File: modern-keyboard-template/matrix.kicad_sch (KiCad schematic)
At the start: 0 parts

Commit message: updated matrix and added dependencies
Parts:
- added D1, D10, D11, D12, D13, D14, D15, D16, D17, D18, D19, D2, D20, D21, D22, D23, D24, D25, D26, D27, D28, D29, D3, D30, D31, D32, D33, D34, D35, D36, D37, D38, D39, D4, D40, D41, D42, D43, D44, D45, D46, D47, D48, D49, D5, D50, D51, D52, D53, D54, D55, D56, D57, D58, D59, D6, D60, D61, D62, D63, D64, D65, D66, D67, D68, D69, D7, D70, D71, D72, D73, D74, D75, D76, D77, D78, D79, D8, D80, D81, D82, D83, D84, D9: D, Diode_SMD:D_SOD-123, symbol Device:D
- added SW? (x84): ~, switches:Kailh_socket_MX, symbol Switch:SW_Push
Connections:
- new net: D12.2 (A), SW?.1
- new net: D19.2 (A), SW?.1
- new net: D42.2 (A), SW?.1
- new net: D4.2 (A), SW?.1
- new net: D58.2 (A), SW?.1
- new net: D57.2 (A), SW?.1
- new net: D10.2 (A), SW?.1
- new net: D33.2 (A), SW?.1
- new net: D48.2 (A), SW?.1
- new net: D5.2 (A), SW?.1
- new net: D80.2 (A), SW?.1
- new net: D53.2 (A), SW?.1
- new net: D73.2 (A), SW?.1
- new net: D31.2 (A), SW?.1
- new net: D83.2 (A), SW?.1
- new net: D66.2 (A), SW?.1
- new net: D69.2 (A), SW?.1
- new net: D35.2 (A), SW?.1
- new net: D50.2 (A), SW?.1
- new net: D18.2 (A), SW?.1
- new net: D75.2 (A), SW?.1
- new net: D54.2 (A), SW?.1
- new net: D52.2 (A), SW?.1
- new net: D13.2 (A), SW?.1
- new net: D15.2 (A), SW?.1
- new net: D29.2 (A), SW?.1
- new net: D71.2 (A), SW?.1
- new net: D67.2 (A), SW?.1
- new net: D44.2 (A), SW?.1
- new net: D55.2 (A), SW?.1
- new net: D17.2 (A), SW?.1
- new net: D62.2 (A), SW?.1
- new net: D37.2 (A), SW?.1
- new net: D6.2 (A), SW?.1
- new net: D84.2 (A), SW?.1
- new net: D2.2 (A), SW?.1
- new net: D25.2 (A), SW?.1
- new net: D68.2 (A), SW?.1
- new net: D30.2 (A), SW?.1
- new net: D26.2 (A), SW?.1
- new net: D81.2 (A), SW?.1
- new net: D60.2 (A), SW?.1
- new net: D74.2 (A), SW?.1
- new net: D46.2 (A), SW?.1
- new net: D72.2 (A), SW?.1
- new net: D56.2 (A), SW?.1
- new net: D49.2 (A), SW?.1
- new net: D7.2 (A), SW?.1
- new net: D41.2 (A), SW?.1
- new net: D70.2 (A), SW?.1
- new net: D23.2 (A), SW?.1
- new net: D9.2 (A), SW?.1
- new net: D20.2 (A), SW?.1
- new net: D76.2 (A), SW?.1
- new net: D78.2 (A), SW?.1
- new net: D38.2 (A), SW?.1
- new net: D63.2 (A), SW?.1
- new net: D51.2 (A), SW?.1
- new net: D47.2 (A), SW?.1
- new net: D24.2 (A), SW?.1
- new net: D3.2 (A), SW?.1
- new net: D27.2 (A), SW?.1
- new net: D36.2 (A), SW?.1
- new net: D21.2 (A), SW?.1
- new net: D32.2 (A), SW?.1
- new net: D64.2 (A), SW?.1
- new net: D40.2 (A), SW?.1
- new net: D77.2 (A), SW?.1
- new net: D28.2 (A), SW?.1
- new net: D14.2 (A), SW?.1
- new net: D65.2 (A), SW?.1
- new net: D82.2 (A), SW?.1
- new net: D1.2 (A), SW?.1
- new net: D45.2 (A), SW?.1
- new net: D59.2 (A), SW?.1
- new net: D34.2 (A), SW?.1
- new net: D61.2 (A), SW?.1
- new net: D16.2 (A), SW?.1
- new net: D39.2 (A), SW?.1
- new net: D22.2 (A), SW?.1
- new net: D11.2 (A), SW?.1
- new net: D43.2 (A), SW?.1
- new net: D79.2 (A), SW?.1
- new net: D8.2 (A), SW?.1
- new net col0: SW?.2, SW?.2, SW?.2, SW?.2, SW?.2
- new net col1: SW?.2, SW?.2, SW?.2, SW?.2
- new net col10: SW?.2, SW?.2, SW?.2, SW?.2, SW?.2, SW?.2
- new net col11: SW?.2, SW?.2, SW?.2, SW?.2, SW?.2, SW?.2
- new net col12: SW?.2, SW?.2, SW?.2, SW?.2, SW?.2
- new net col13: SW?.2, SW?.2, SW?.2, SW?.2, SW?.2
- new net col14: SW?.2, SW?.2, SW?.2, SW?.2, SW?.2
- new net col15: SW?.2, SW?.2, SW?.2, SW?.2, SW?.2, SW?.2
- new net col2: SW?.2, SW?.2, SW?.2, SW?.2, SW?.2
- new net col3: SW?.2, SW?.2, SW?.2, SW?.2, SW?.2, SW?.2
- new net col4: SW?.2, SW?.2, SW?.2, SW?.2, SW?.2
- new net col5: SW?.2, SW?.2, SW?.2, SW?.2, SW?.2
- new net col6: SW?.2, SW?.2, SW?.2, SW?.2, SW?.2, SW?.2
- new net col7: SW?.2, SW?.2, SW?.2, SW?.2, SW?.2
- new net col8: SW?.2, SW?.2, SW?.2, SW?.2, SW?.2
- new net col9: SW?.2, SW?.2, SW?.2, SW?.2, SW?.2
- new net row0: D1.1 (K), D10.1 (K), D15.1 (K), D21.1 (K), D26.1 (K), D31.1 (K), D37.1 (K), D42.1 (K), D47.1 (K), D52.1 (K), D58.1 (K), D6.1 (K), D64.1 (K), D69.1 (K), D74.1 (K), D79.1 (K)
- new net row1: D11.1 (K), D16.1 (K), D2.1 (K), D22.1 (K), D27.1 (K), D32.1 (K), D38.1 (K), D43.1 (K), D48.1 (K), D53.1 (K), D59.1 (K), D65.1 (K), D7.1 (K), D75.1 (K), D80.1 (K)
- new net row2: D12.1 (K), D17.1 (K), D23.1 (K), D28.1 (K), D3.1 (K), D33.1 (K), D39.1 (K), D44.1 (K), D49.1 (K), D54.1 (K), D60.1 (K), D66.1 (K), D70.1 (K), D76.1 (K), D81.1 (K)
- new net row3: D13.1 (K), D18.1 (K), D24.1 (K), D29.1 (K), D34.1 (K), D4.1 (K), D40.1 (K), D45.1 (K), D50.1 (K), D55.1 (K), D61.1 (K), D67.1 (K), D71.1 (K), D82.1 (K)
- new net row4: D14.1 (K), D19.1 (K), D25.1 (K), D30.1 (K), D35.1 (K), D41.1 (K), D46.1 (K), D51.1 (K), D56.1 (K), D62.1 (K), D72.1 (K), D77.1 (K), D8.1 (K), D83.1 (K)
- new net row5: D20.1 (K), D36.1 (K), D5.1 (K), D57.1 (K), D63.1 (K), D68.1 (K), D73.1 (K), D78.1 (K), D84.1 (K), D9.1 (K)

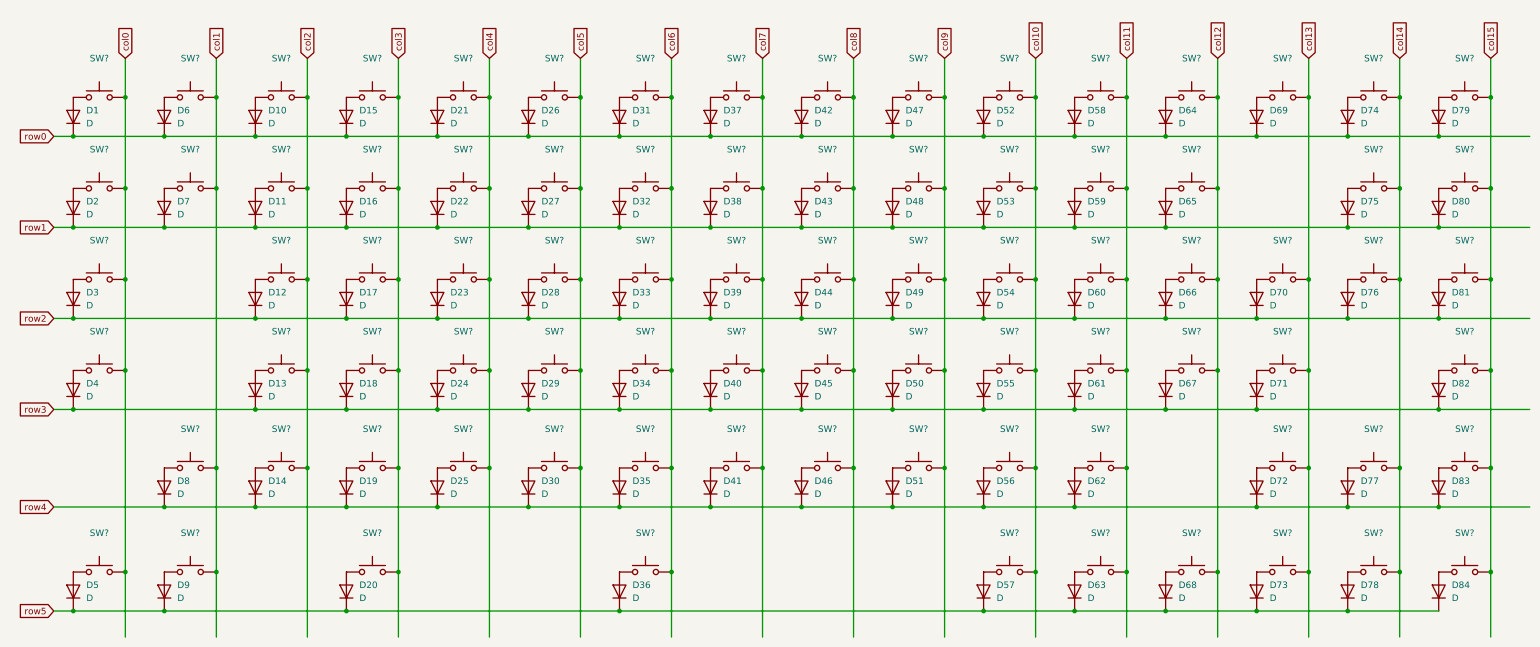
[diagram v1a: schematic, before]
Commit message: updated pcb w/ switches
need to revisit this entire design tbh
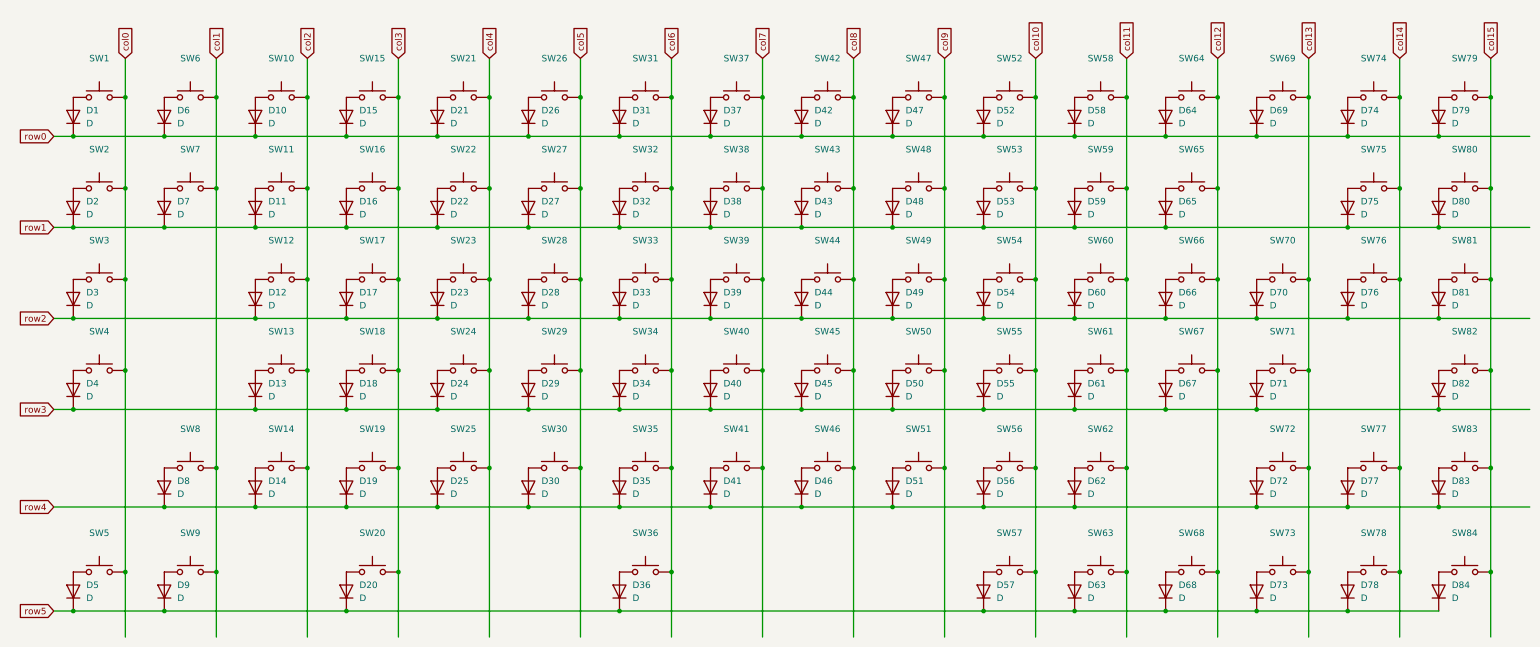
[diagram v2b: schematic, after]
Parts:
- gave numbers to parts that had none: 84

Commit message: added layout file, router keys
added layout file in /dependencies
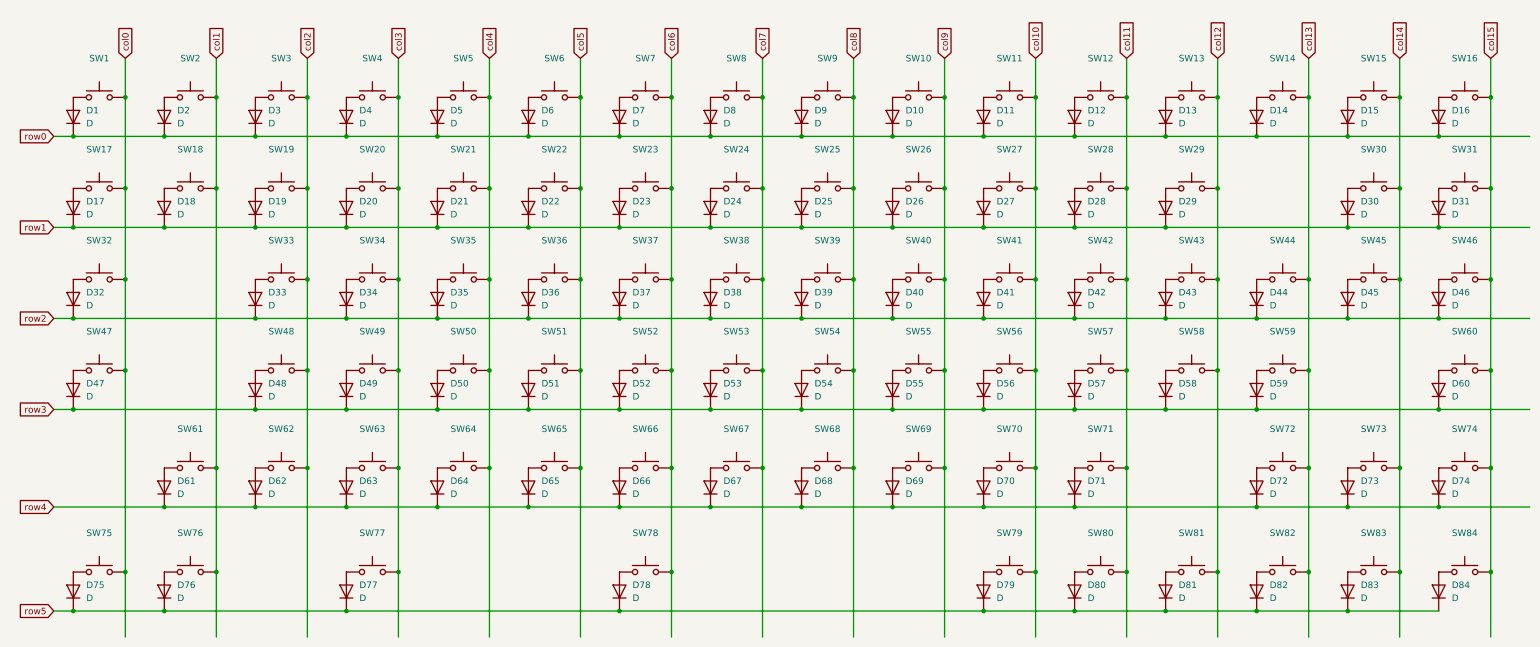
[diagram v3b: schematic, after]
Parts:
- renumbered D47 to D10, D52 to D11, D58 to D12, D64 to D13, D69 to D14, D74 to D15, D79 to D16, D2 to D17, D7 to D18, D11 to D19, D6 to D2, D16 to D20, D22 to D21, D27 to D22, D32 to D23, D38 to D24, D43 to D25, D48 to D26, D53 to D27, D59 to D28, D65 to D29, D10 to D3, D75 to D30, D80 to D31, D3 to D32, D12 to D33, D17 to D34, D23 to D35, D28 to D36, D33 to D37, D39 to D38, D44 to D39, D15 to D4, D49 to D40, D54 to D41, D60 to D42, D66 to D43, D70 to D44, D76 to D45, D81 to D46, D4 to D47, D13 to D48, D18 to D49, D21 to D5, D24 to D50, D29 to D51, D34 to D52, D40 to D53, D45 to D54, D50 to D55, D55 to D56, D61 to D57, D67 to D58, D71 to D59, D26 to D6, D82 to D60, D8 to D61, D14 to D62, D19 to D63, D25 to D64, D30 to D65, D35 to D66, D41 to D67, D46 to D68, D51 to D69, D31 to D7, D56 to D70, D62 to D71, D77 to D73, D83 to D74, D5 to D75, D9 to D76, D20 to D77, D36 to D78, D57 to D79, D37 to D8, D63 to D80, D68 to D81, D73 to D82, D78 to D83, D42 to D9, SW47 to SW10, SW52 to SW11, SW58 to SW12, SW64 to SW13, SW69 to SW14, SW74 to SW15, SW79 to SW16, SW2 to SW17, SW7 to SW18, SW11 to SW19, SW6 to SW2, SW16 to SW20, SW22 to SW21, SW27 to SW22, SW32 to SW23, SW38 to SW24, SW43 to SW25, SW48 to SW26, SW53 to SW27, SW59 to SW28, SW65 to SW29, SW10 to SW3, SW75 to SW30, SW80 to SW31, SW3 to SW32, SW12 to SW33, SW17 to SW34, SW23 to SW35, SW28 to SW36, SW33 to SW37, SW39 to SW38, SW44 to SW39, SW15 to SW4, SW49 to SW40, SW54 to SW41, SW60 to SW42, SW66 to SW43, SW70 to SW44, SW76 to SW45, SW81 to SW46, SW4 to SW47, SW13 to SW48, SW18 to SW49, SW21 to SW5, SW24 to SW50, SW29 to SW51, SW34 to SW52, SW40 to SW53, SW45 to SW54, SW50 to SW55, SW55 to SW56, SW61 to SW57, SW67 to SW58, SW71 to SW59, SW26 to SW6, SW82 to SW60, SW8 to SW61, SW14 to SW62, SW19 to SW63, SW25 to SW64, SW30 to SW65, SW35 to SW66, SW41 to SW67, SW46 to SW68, SW51 to SW69, SW31 to SW7, SW56 to SW70, SW62 to SW71, SW77 to SW73, SW83 to SW74, SW5 to SW75, SW9 to SW76, SW20 to SW77, SW36 to SW78, SW57 to SW79, SW37 to SW8, SW63 to SW80, SW68 to SW81, SW73 to SW82, SW78 to SW83, SW42 to SW9
